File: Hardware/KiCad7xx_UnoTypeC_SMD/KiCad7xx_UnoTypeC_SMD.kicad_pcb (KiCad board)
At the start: 2 copper layers, 68.6 x 53.3 mm, 76 parts, among them J1 -, J2 -, T1 FDN340P, U1 NCP1117ST50T3G, U2 LP2985-33DBVR, U3 16U2, U4 ATMEGA328P-MU, U5 LMV358IDGKR, X1 POWERSUPPLY_DC21MMX, X2 USB-B_TH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

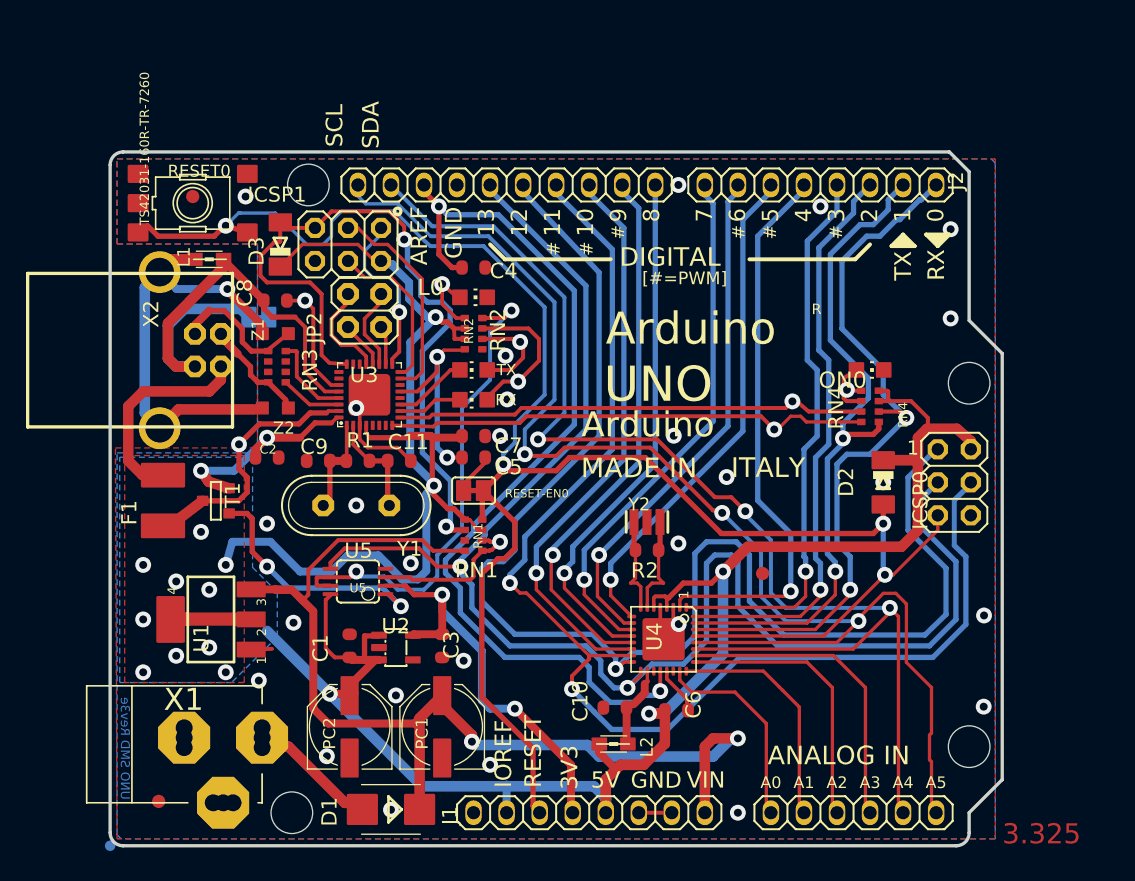
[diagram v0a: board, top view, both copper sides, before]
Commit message: feat: 取り付け穴が消えてしまう為,新たにM3_IOS14580を追加
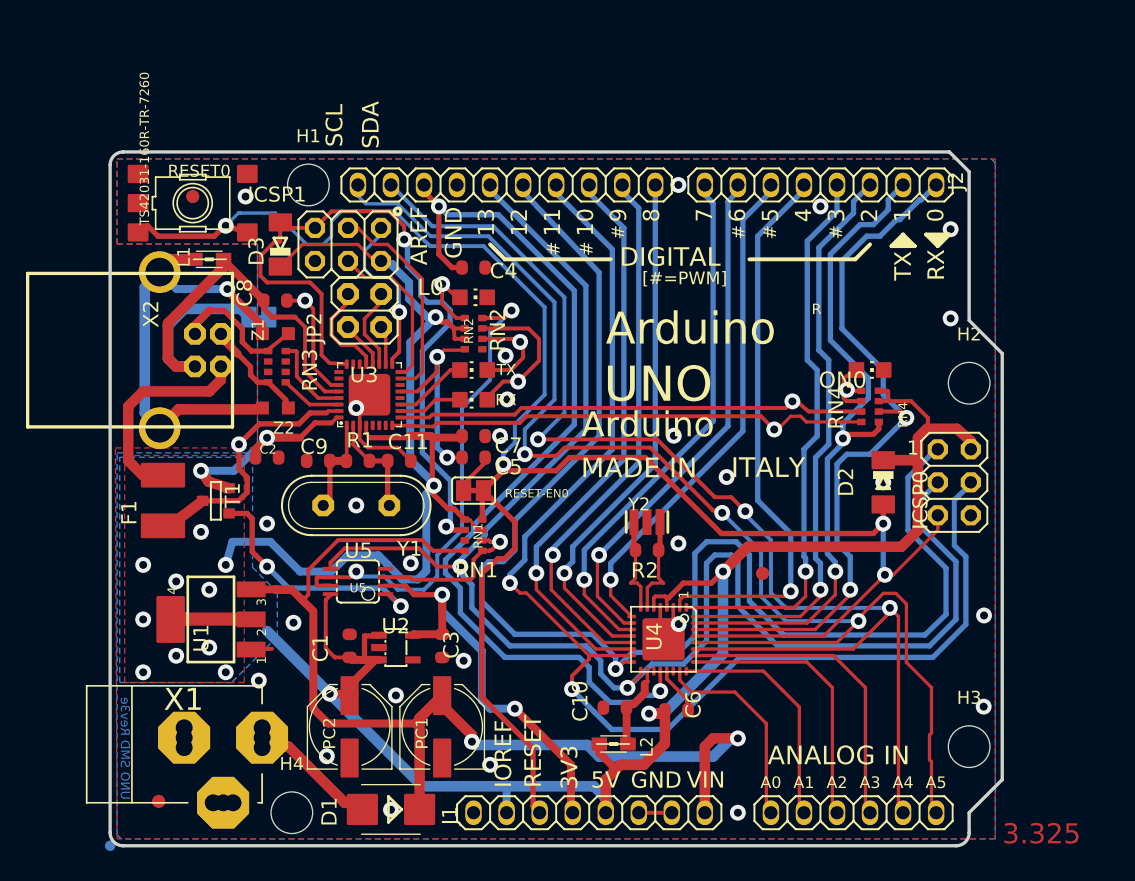
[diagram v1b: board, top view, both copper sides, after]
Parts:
- removed @HOLE0, @HOLE1, @HOLE2, @HOLE3: , 
- removed FRAME1: DNP, FRAME
- added H1: MountingHole, MountingHole:MountingHole_3.2mm_M3_ISO14580, F.Cu at (129.5, 80.9)
- added H2: MountingHole, MountingHole:MountingHole_3.2mm_M3_ISO14580, F.Cu at (180.3, 96.1)
- added H3: MountingHole, MountingHole:MountingHole_3.2mm_M3_ISO14580, F.Cu at (180.3, 124.1)
- added H4: MountingHole, MountingHole:MountingHole_3.2mm_M3_ISO14580, F.Cu at (128.2, 129.1)
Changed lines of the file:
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@@
       (net 55 "5-GND") (solder_mask_margin 0.0508) (solder_paste_margin -0.07) (thermal_bridge_angle 45))
   )
-  (footprint "FRAME" (layer "F.Cu")
-    (at 92.7111 136.1736)
-    (fp_text reference "FRAME1" (at 0 0) (layer "F.SilkS") hide
-        (effects (font (size 1.27 1.27) (thickness 0.15)))
-    )
-    (fp_text value "DNP" (at 0 0) (layer "F.Fab") hide
-        (effects (font (size 1.27 1.27) (thickness 0.15)))
-    )
-    (fp_text user "Reference Designs ARE PROVIDED \"AS IS\" AND \"WITH ALL FAULTS. Arduino SA DISCLAIMS ALL OTHER WARRANTIES, EXPRESS OR IMPLIED,\nREGARDING PRODUCTS, INCLUDING BUT NOT LIMITED TO, ANY IMPLIED WARRANTIES OF MERCHANTABILITY OR FITNESS FOR A \nPARTICULAR PURPOSE \nArduino SA may make changes to specifications and product descriptions at any time, without notice. The Customer must not\nrely on the absence or characteristics of any features or instructions marked \"reserved\" or \"undefined.\" Arduino SA reserves\nthese for future definition and shall have no responsibility whatsoever for conflicts or incompatibilities arising from future changes to them.\nThe product information on the Web Site or Materials is subject to change without notice. Do not finalize a design with this info\n\nARDUINO and other Arduino brands and logos and Trademarks of Arduino SA. All Arduino SA Trademarks cannot be used without owner's formal permission\n\nThis file is licensed under : CC-SA-BY-NC" (at 0 17.78) (layer "F.Fab")
-        (effects (font (size 1.1684 1.1684) (thickness 0.1016)) (justify left bottom))
-    )
-  )
   (footprint "TP-SP" (layer "F.Cu")
     (at 165.2651 99.6696)
@@
       (net 22 "USBVCC") (solder_mask_margin 0.0508) (solder_paste_margin -0.0508) (zone_connect 2) (thermal_bridge_angle 45))
   )
-  (footprint "" (layer "F.Cu")
-    (at 128.1811 129.1336)
-    (fp_text reference "@HOLE3" (at 0 0) (layer "F.SilkS") hide
-        (effects (font (size 1.27 1.27) (thickness 0.15)))
-    )
-    (fp_text value "" (at 0 0) (layer "F.SilkS")
-        (effects (font (size 1.27 1.27) (thickness 0.15)))
-    )
-    (pad "" np_thru_hole circle (at 0 0) (size 3.2 3.2) (drill 3.2) (layers "*.Cu" "*.Mask"))
-  )
   (footprint "1X18-CUSTOM" (layer "F.Cu")
     (at 159.9311 80.8736 180)
@@
       (net 2 "GND") (solder_mask_margin 0.0508) (solder_paste_margin -0.07) (thermal_bridge_angle 45))
   )
+  (footprint "MountingHole:MountingHole_3.2mm_M3_ISO14580" (layer "F.Cu")
+    (at 180.2511 124.0536)
+    (descr "Mounting Hole 3.2mm, no annular, M3, ISO14580")
+    (tags "mounting hole 3.2mm no annular m3 iso14580")
+    (property "Sheetfile" "KiCad7xx_UnoTypeC_SMD.kicad_sch")
+    (property "Sheetname" "")
+    (property "ki_description" "Mounting Hole without connection")
+    (property "ki_keywords" "mounting hole")
+    (attr exclude_from_pos_files)
+    (fp_text reference "H3" (at 0 -3.75) (layer "F.SilkS")
+        (effects (font (size 1 1) (thickness 0.15)))
+    )
+    (fp_text value "MountingHole" (at 0 3.75) (layer "F.Fab")
+        (effects (font (size 1 1) (thickness 0.15)))
+    )
+    (fp_text user "${REFERENCE}" (at 0 0) (layer "F.Fab")
+        (effects (font (size 1 1) (thickness 0.15)))
+    )
+    (fp_circle (center 0 0) (end 2.75 0)
+      (stroke (width 0.15) (type solid)) (fill none) (layer "Cmts.User"))
+    (fp_circle (center 0 0) (end 3 0)
+      (stroke (width 0.05) (type solid)) (fill none) (layer "F.CrtYd"))
+    (pad "" np_thru_hole circle (at 0 0) (size 3.2 3.2) (drill 3.2) (layers "*.Cu" "*.Mask"))
+  )
+  (footprint "MountingHole:MountingHole_3.2mm_M3_ISO14580" (layer "F.Cu")
+    (at 180.2511 96.1136)
+    (descr "Mounting Hole 3.2mm, no annular, M3, ISO14580")
+    (tags "mounting hole 3.2mm no annular m3 iso14580")
+    (property "Sheetfile" "KiCad7xx_UnoTypeC_SMD.kicad_sch")
+    (property "Sheetname" "")
+    (property "ki_description" "Mounting Hole without connection")
+    (property "ki_keywords" "mounting hole")
+    (attr exclude_from_pos_files)
+    (fp_text reference "H2" (at 0 -3.75) (layer "F.SilkS")
+        (effects (font (size 1 1) (thickness 0.15)))
+    )
+    (fp_text value "MountingHole" (at 0 3.75) (layer "F.Fab")
+        (effects (font (size 1 1) (thickness 0.15)))
+    )
+    (fp_text user "${REFERENCE}" (at 0 0) (layer "F.Fab")
+        (effects (font (size 1 1) (thickness 0.15)))
+    )
+    (fp_circle (center 0 0) (end 2.75 0)
+      (stroke (width 0.15) (type solid)) (fill none) (layer "Cmts.User"))
+    (fp_circle (center 0 0) (end 3 0)
+      (stroke (width 0.05) (type solid)) (fill none) (layer "F.CrtYd"))
+    (pad "" np_thru_hole circle (at 0 0) (size 3.2 3.2) (drill 3.2) (layers "*.Cu" "*.Mask"))
+  )
   (footprint "CHIP-LED0805" (layer "F.Cu")
     (at 142.1511 89.5096 -90)
@@
       (net 56 "N$1") (solder_mask_margin 0.0508) (solder_paste_margin -0.0508) (zone_connect 2) (thermal_bridge_angle 45))
   )
-  (footprint "" (layer "F.Cu")
-    (at 180.2511 96.1136)
-    (fp_text reference "@HOLE0" (at 0 0) (layer "F.SilkS") hide
-        (effects (font (size 1.27 1.27) (thickness 0.15)))
-    )
-    (fp_text value "" (at 0 0) (layer "F.SilkS")
-        (effects (font (size 1.27 1.27) (thickness 0.15)))
-    )
-    (pad "" np_thru_hole circle (at 0 0) (size 3.2 3.2) (drill 3.2) (layers "*.Cu" "*.Mask"))
-  )
-  (footprint "" (layer "F.Cu")
-    (at 180.2511 124.0536)
-    (fp_text reference "@HOLE1" (at 0 0) (layer "F.SilkS") hide
-        (effects (font (size 1.27 1.27) (thickness 0.15)))
-    )
-    (fp_text value "" (at 0 0) (layer "F.SilkS")
-        (effects (font (size 1.27 1.27) (thickness 0.15)))
-    )
-    (pad "" np_thru_hole circle (at 0 0) (size 3.2 3.2) (drill 3.2) (layers "*.Cu" "*.Mask"))
-  )
   (footprint "PANASONIC_D" (layer "F.Cu")
     (at 139.7381 122.5296 90)
@@
       (net 44 "A5/SCL") (solder_mask_margin 0.0508) (thermal_bridge_angle 45))
   )
+  (footprint "MountingHole:MountingHole_3.2mm_M3_ISO14580" (layer "F.Cu")
+    (at 129.4511 80.8736)
+    (descr "Mounting Hole 3.2mm, no annular, M3, ISO14580")
+    (tags "mounting hole 3.2mm no annular m3 iso14580")
+    (property "Sheetfile" "KiCad7xx_UnoTypeC_SMD.kicad_sch")
+    (property "Sheetname" "")
+    (property "ki_description" "Mounting Hole without connection")
+    (property "ki_keywords" "mounting hole")
+    (attr exclude_from_pos_files)
+    (fp_text reference "H1" (at 0 -3.75) (layer "F.SilkS")
+        (effects (font (size 1 1) (thickness 0.15)))
+    )
+    (fp_text value "MountingHole" (at 0 3.75) (layer "F.Fab")
+        (effects (font (size 1 1) (thickness 0.15)))
+    )
+    (fp_text user "${REFERENCE}" (at 0 0) (layer "F.Fab")
+        (effects (font (size 1 1) (thickness 0.15)))
+    )
+    (fp_circle (center 0 0) (end 2.75 0)
+      (stroke (width 0.15) (type solid)) (fill none) (layer "Cmts.User"))
+    (fp_circle (center 0 0) (end 3 0)
+      (stroke (width 0.05) (type solid)) (fill none) (layer "F.CrtYd"))
+    (pad "" np_thru_hole circle (at 0 0) (size 3.2 3.2) (drill 3.2) (layers "*.Cu" "*.Mask"))
+  )
   (footprint "TP-SP" (layer "F.Cu")
     (at 129.1971 89.7636)
@@
       (net 10 "N$35") (solder_mask_margin 0.0508) (solder_paste_margin -0.0508) (zone_connect 2) (thermal_bridge_angle 45))
   )
+  (footprint "MountingHole:MountingHole_3.2mm_M3_ISO14580" (layer "F.Cu")
+    (at 128.1811 129.1336)
+    (descr "Mounting Hole 3.2mm, no annular, M3, ISO14580")
+    (tags "mounting hole 3.2mm no annular m3 iso14580")
+    (property "Sheetfile" "KiCad7xx_UnoTypeC_SMD.kicad_sch")
+    (property "Sheetname" "")
+    (property "ki_description" "Mounting Hole without connection")
+    (property "ki_keywords" "mounting hole")
+    (attr exclude_from_pos_files)
+    (fp_text reference "H4" (at 0 -3.75) (layer "F.SilkS")
+        (effects (font (size 1 1) (thickness 0.15)))
+    )
+    (fp_text value "MountingHole" (at 0 3.75) (layer "F.Fab")
+        (effects (font (size 1 1) (thickness 0.15)))
+    )
+    (fp_text user "${REFERENCE}" (at 0 0) (layer "F.Fab")
+        (effects (font (size 1 1) (thickness 0.15)))
+    )
+    (fp_circle (center 0 0) (end 2.75 0)
+      (stroke (width 0.15) (type solid)) (fill none) (layer "Cmts.User"))
+    (fp_circle (center 0 0) (end 3 0)
+      (stroke (width 0.05) (type solid)) (fill none) (layer "F.CrtYd"))
+    (pad "" np_thru_hole circle (at 0 0) (size 3.2 3.2) (drill 3.2) (layers "*.Cu" "*.Mask"))
+  )
   (footprint "QS" (layer "F.Cu")
     (at 133.1341 105.5116 180)
@@
       (net 11 "N$36") (solder_mask_margin 0.0508) (solder_paste_margin -0.0508) (zone_connect 2) (thermal_bridge_angle 45))
   )
-  (footprint "" (layer "F.Cu")
-    (at 129.4511 80.8736)
-    (fp_text reference "@HOLE2" (at 0 0) (layer "F.SilkS") hide
-        (effects (font (size 1.27 1.27) (thickness 0.15)))
-    )
-    (fp_text value "" (at 0 0) (layer "F.SilkS")
-        (effects (font (size 1.27 1.27) (thickness 0.15)))
-    )
-    (pad "" np_thru_hole circle (at 0 0) (size 3.2 3.2) (drill 3.2) (layers "*.Cu" "*.Mask"))
-  )
   (footprint "SOT-23" (layer "F.Cu")
     (at 122.3391 105.1306 -90)
@@
     (connect_pads (clearance 0.4064))
     (min_thickness 0.1016) (filled_areas_thickness no)
-    (fill (thermal_gap 0.2532) (thermal_bridge_width 0.2532))
+    (fill yes (thermal_gap 0.2532) (thermal_bridge_width 0.2532))
     (polygon
       (pts
@@
     (connect_pads (clearance 0.4064))
     (min_thickness 0.1016) (filled_areas_thickness no)
-    (fill (thermal_gap 0.2532) (thermal_bridge_width 0.2532))
+    (fill yes (thermal_gap 0.2532) (thermal_bridge_width 0.2532))
     (polygon
       (pts

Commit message: feat: Type-Cコネクタの回路を追加
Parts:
- C1, C10, C11, C2, C3, C4, C5, C6, C7, C8, C9: footprint C0603-ROUND -> UNOSMD_V3:C0603-ROUND
- D1: footprint SMB -> UNOSMD_V3:SMB
- D2, D3: footprint MINIMELF -> UNOSMD_V3:MINIMELF
- F1: footprint L1812 -> UNOSMD_V3:L1812
- FD1, FD2, FD3: footprint FD-1-1.5 -> UNOSMD_V3:FD-1-1.5
- GROUND0, RESET-EN0: footprint SJ -> UNOSMD_V3:SJ
- H1, H2, H3, H4: footprint MountingHole:MountingHole_3.2mm_M3_ISO14580 -> UNOSMD_V3:MountingHole_3.2mm_M3_ISO14580
- ICSP0, ICSP1: footprint 2X03 -> UNOSMD_V3:2X03
- J1: footprint 1X14-CUSTOM -> UNOSMD_V3:1X14-CUSTOM
- J2: footprint 1X18-CUSTOM -> UNOSMD_V3:1X18-CUSTOM
- JP2: footprint 2X02 -> UNOSMD_V3:2X02
- L0, ON0, RX0, TX0: footprint CHIP-LED0805 -> UNOSMD_V3:CHIP-LED0805
- L1, L2: footprint 0805 -> UNOSMD_V3:0805
- ORIGIN0, TP_5V1, TP_CMP0, TP_DTR0, TP_GATE0, TP_LCMD0, TP_LL0, TP_MISO2, TP_MOSI2, TP_ONL0, TP_RESET2, TP_RX0, TP_RXL0, TP_SCK2, TP_TX0, TP_TXL0, TP_USBVCC0, TP_USH0, TP_VUCAP0: footprint TP-SP -> UNOSMD_V3:TP-SP
- PC1, PC2: footprint PANASONIC_D -> UNOSMD_V3:PANASONIC_D
- R1, R2: footprint R0603-ROUND -> UNOSMD_V3:R0603-ROUND
- RESET0: footprint TS42 -> UNOSMD_V3:TS42
- RN1, RN2, RN3, RN4: footprint CAY16 -> UNOSMD_V3:CAY16
- T1: footprint SOT-23 -> UNOSMD_V3:SOT-23
- U1: footprint SOT223 -> UNOSMD_V3:SOT223
- U2: footprint SOT23-DBV -> UNOSMD_V3:SOT23-DBV
- U3: footprint ATMEL_QFN32 -> UNOSMD_V3:ATMEL_QFN32
- U4: footprint MLF32 -> UNOSMD_V3:MLF32
- U5: footprint MSOP08 -> UNOSMD_V3:MSOP08
- X1: footprint POWERSUPPLY_DC-21MM -> UNOSMD_V3:POWERSUPPLY_DC-21MM
- X2: footprint PN61729 -> UNOSMD_V3:PN61729
- Y1: footprint QS -> UNOSMD_V3:QS
- Y2: footprint RESONATOR -> UNOSMD_V3:RESONATOR
- Z1, Z2: footprint CT_CN0603 -> UNOSMD_V3:CT_CN0603
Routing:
- net UGND: track 39.2 -> 0.00 mm
- net GND: track 22.1 -> 61.3 mm
